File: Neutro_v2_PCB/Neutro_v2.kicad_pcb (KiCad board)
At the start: 4 copper layers, 101.6 x 63.5 mm, 44 parts, among them J1 SparkFun_Lipo_Converter, J2 Conn_Coaxial, U1 Adafruit_GPS, U2 RFM96W-433S2_1, U3 MS5803-01BA, U4 BNO080, U5 DS3231M_1

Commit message: update v2 pcb
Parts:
- moved TP1 0.25 mm to (161.9, 127.0), turned to 0 degrees
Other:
- board text added: "BOOTN"
- board text added: "CS"
- board text added: "GND"
- board text added: "MISO"
- board text added: "MOSI"
- board text added: "SCL0"
- board text added: "SCL1"
- board text added: "SCLK"
- board text added: "SDA0"
- board text added: "SDA1"
- board text added: "v2"
- board text removed: "v1"

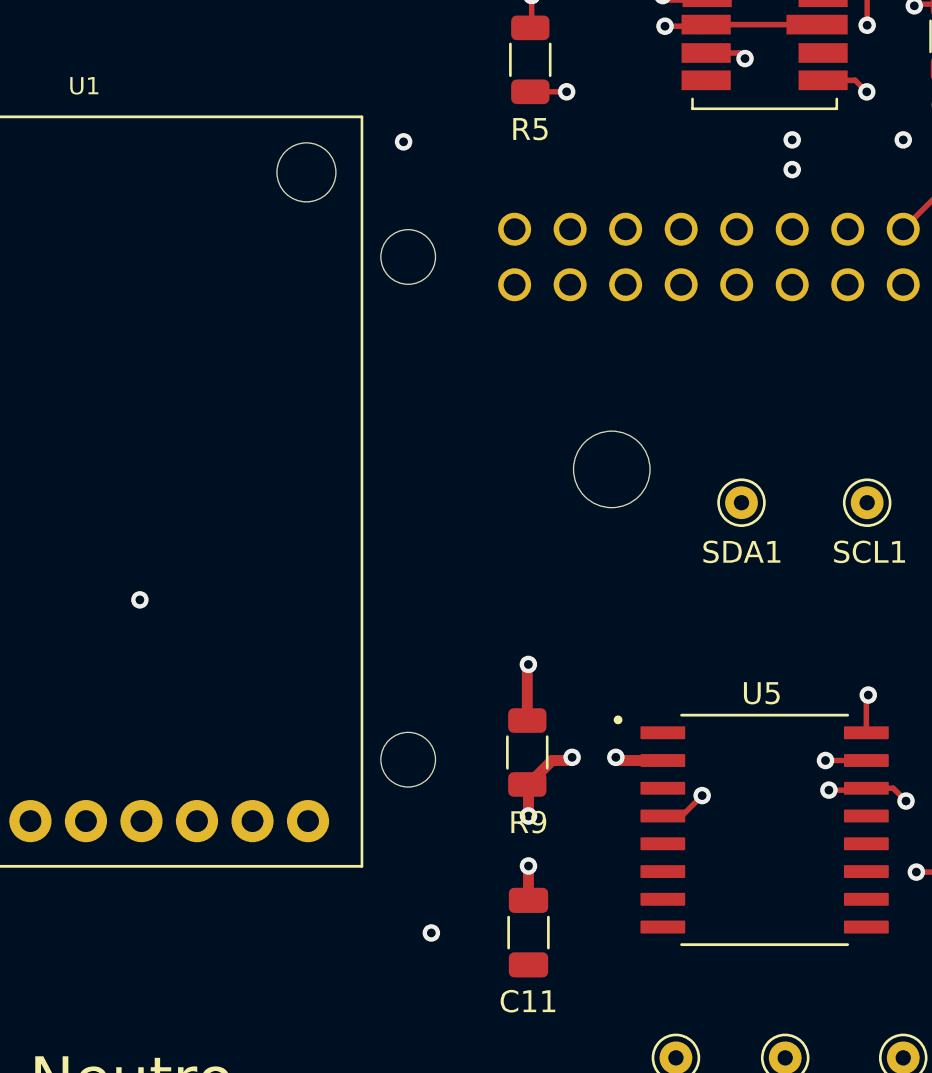
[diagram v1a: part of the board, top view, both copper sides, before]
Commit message: verified gps module footprint
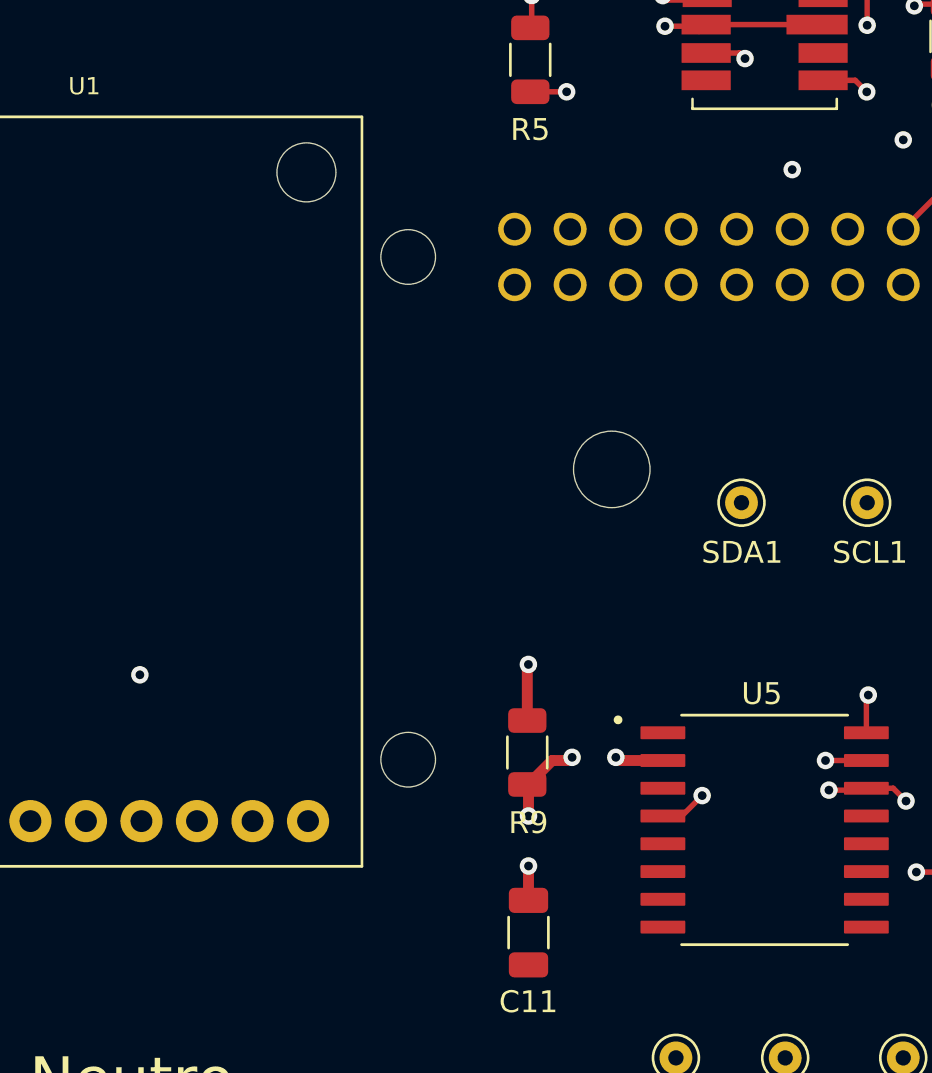
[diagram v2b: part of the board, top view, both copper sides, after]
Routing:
- net +BATT: track 53.2 -> 51.8 mm, vias 4 -> 3
- net TX: vias 3 -> 1
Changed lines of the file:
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@@
   (segment (start 150.7315 82.804) (end 150.7315 88.2165) (width 0.25) (layer "In1.Cu") (net 5))
   (via (at 147.32 86.36) (size 0.8) (drill 0.4) (layers "F.Cu" "B.Cu") (net 6))
-  (via (at 117.475 106.045) (size 0.8) (drill 0.4) (layers "F.Cu" "B.Cu") (net 6))
+  (via (at 117.475 109.474) (size 0.8) (drill 0.4) (layers "F.Cu" "B.Cu") (net 6))
   (via (at 156.21 86.36) (size 0.8) (drill 0.4) (layers "F.Cu" "B.Cu") (net 6))
   (segment (start 172.532 86.36) (end 175.26 89.088) (width 0.25) (layer "In1.Cu") (net 6))
@@
   (segment (start 130.175 86.36) (end 147.32 86.36) (width 0.25) (layer "In1.Cu") (net 6))
   (segment (start 156.21 86.36) (end 172.532 86.36) (width 0.25) (layer "In1.Cu") (net 6))
-  (segment (start 117.475 106.045) (end 117.475 99.06) (width 0.25) (layer "In1.Cu") (net 6))
-  (segment (start 117.548 106.118) (end 117.475 106.045) (width 0.25) (layer "In2.Cu") (net 6))
+  (segment (start 117.475 109.474) (end 117.475 99.06) (width 0.25) (layer "In1.Cu") (net 6))
+  (segment (start 117.548 109.547) (end 117.548 116.168) (width 0.25) (layer "In2.Cu") (net 6))
   (segment (start 156.21 86.36) (end 147.32 86.36) (width 0.25) (layer "In2.Cu") (net 6))
-  (segment (start 117.548 116.168) (end 117.548 106.118) (width 0.25) (layer "In2.Cu") (net 6))
-  (via (at 147.32 85.0005) (size 0.8) (drill 0.4) (layers "F.Cu" "B.Cu") (net 7))
-  (via (at 129.54 85.09) (size 0.8) (drill 0.4) (layers "F.Cu" "B.Cu") (net 7))
+  (segment (start 117.475 109.474) (end 117.548 109.547) (width 0.25) (layer "In2.Cu") (net 6))
   (via (at 152.4 85.0005) (size 0.8) (drill 0.4) (layers "F.Cu" "B.Cu") (net 7))
   (segment (start 152.4 85.0005) (end 153.3265 85.0005) (width 0.25) (layer "In1.Cu") (net 7))
   (segment (start 153.3265 85.0005) (end 155.702 87.376) (width 0.25) (layer "In1.Cu") (net 7))
   (segment (start 171.008 87.376) (end 172.72 89.088) (width 0.25) (layer "In1.Cu") (net 7))
-  (segment (start 147.32 85.0005) (end 147.2305 85.09) (width 0.25) (layer "In1.Cu") (net 7))
-  (segment (start 147.2305 85.09) (end 129.54 85.09) (width 0.25) (layer "In1.Cu") (net 7))
   (segment (start 155.702 87.376) (end 171.008 87.376) (width 0.25) (layer "In1.Cu") (net 7))
-  (segment (start 115.008 99.622) (end 129.54 85.09) (width 0.25) (layer "In2.Cu") (net 7))
-  (segment (start 115.008 116.168) (end 115.008 99.622) (width 0.25) (layer "In2.Cu") (net 7))
-  (segment (start 152.4 85.0005) (end 147.32 85.0005) (width 0.25) (layer "In2.Cu") (net 7))
+  (segment (start 129.6295 85.0005) (end 115.008 99.622) (width 0.25) (layer "In2.Cu") (net 7))
+  (segment (start 152.4 85.0005) (end 129.6295 85.0005) (width 0.25) (layer "In2.Cu") (net 7))
+  (segment (start 115.008 99.622) (end 115.008 116.168) (width 0.25) (layer "In2.Cu") (net 7))
   (segment (start 142.265 115.935) (end 143.2 115) (width 0.25) (layer "F.Cu") (net 8))
   (segment (start 141.403 115.935) (end 142.265 115.935) (width 0.25) (layer "F.Cu") (net 8))
@@
   (via (at 153 118.5) (size 0.8) (drill 0.4) (layers "F.Cu" "B.Cu") (net 22))
   (via (at 152.527 115.25) (size 0.8) (drill 0.4) (layers "F.Cu" "B.Cu") (net 22))
-  (via (at 130.81 121.285) (size 0.8) (drill 0.4) (layers "F.Cu" "B.Cu") (net 22))
   (via (at 149 114.75) (size 0.8) (drill 0.4) (layers "F.Cu" "B.Cu") (net 22))
-  (segment (start 115.045 121.285) (end 109.928 116.168) (width 0.25) (layer "In1.Cu") (net 22))
   (segment (start 152.527 115.25) (end 152.527 118.027) (width 0.25) (layer "In1.Cu") (net 22))
   (segment (start 152.527 118.027) (end 153 118.5) (width 0.25) (layer "In1.Cu") (net 22))
-  (segment (start 115.045 121.285) (end 130.81 121.285) (width 0.25) (layer "In1.Cu") (net 22))
-  (segment (start 130.81 121.285) (end 142.465 121.285) (width 0.25) (layer "In2.Cu") (net 22))
-  (segment (start 142.465 121.285) (end 149 114.75) (width 0.25) (layer "In2.Cu") (net 22))
+  (segment (start 109.928 116.168) (end 113.394 119.634) (width 0.25) (layer "In2.Cu") (net 22))
+  (segment (start 113.394 119.634) (end 144.116 119.634) (width 0.25) (layer "In2.Cu") (net 22))
+  (segment (start 144.116 119.634) (end 149 114.75) (width 0.25) (layer "In2.Cu") (net 22))
   (segment (start 137.16 113.395) (end 136.3365 113.395) (width 0.5) (layer "F.Cu") (net 23))
   (segment (start 141.395 113.395) (end 139.319 113.395) (width 0.5) (layer "F.Cu") (net 23))
@@
   (segment (start 138.43125 75.43125) (end 136.7375 75.43125) (width 0.5) (layer "B.Cu") (net 43))
   (segment (start 141.4 78.4) (end 138.43125 75.43125) (width 0.5) (layer "B.Cu") (net 43))
-  (segment (start 112.468 116.168) (end 135.818278 92.817722) (width 0.25) (layer "In1.Cu") (net 53))
-  (segment (start 135.818278 92.817722) (end 138.510278 92.817722) (width 0.25) (layer "In1.Cu") (net 53))
-  (segment (start 138.510278 92.817722) (end 139.7 91.628) (width 0.25) (layer "In1.Cu") (net 53))
+  (segment (start 112.468 116.168) (end 134.91 93.726) (width 0.25) (layer "In1.Cu") (net 53))
+  (segment (start 134.91 93.726) (end 137.602 93.726) (width 0.25) (layer "In1.Cu") (net 53))
+  (segment (start 137.602 93.726) (end 139.7 91.628) (width 0.25) (layer "In1.Cu") (net 53))
   (segment (start 169.4625 77) (end 175.8 77) (width 0.25) (layer "F.Cu") (net 57))
   (segment (start 169.4625 77.115) (end 169.6625 76.915) (width 0.25) (layer "F.Cu") (net 57))
@@
   (via (at 178.8 113.2) (size 0.8) (drill 0.4) (layers "F.Cu" "B.Cu") (free) (net 63))
   (via (at 178.7 120.8) (size 0.8) (drill 0.4) (layers "F.Cu" "B.Cu") (free) (net 63))
-  (segment (start 137.16 95.885) (end 125.168 107.877) (width 0.25) (layer "In2.Cu") (net 64))
-  (segment (start 137.16 91.628) (end 137.16 95.885) (width 0.25) (layer "In2.Cu") (net 64))
-  (segment (start 125.168 107.877) (end 125.168 116.168) (width 0.25) (layer "In2.Cu") (net 64))
+  (segment (start 137.16 95.758) (end 125.168 107.75) (width 0.25) (layer "In2.Cu") (net 64))
+  (segment (start 125.168 107.75) (end 125.168 116.168) (width 0.25) (layer "In2.Cu") (net 64))
+  (segment (start 137.16 91.628) (end 137.16 95.758) (width 0.25) (layer "In2.Cu") (net 64))
   (zone (net 1) (net_name "+3.3V") (layer "F.Cu") (hatch edge 0.508)
     (priority 1)
